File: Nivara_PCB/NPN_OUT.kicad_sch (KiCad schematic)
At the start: 0 parts

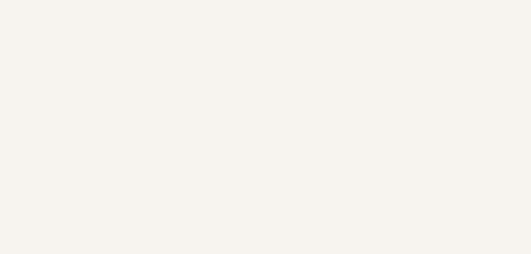
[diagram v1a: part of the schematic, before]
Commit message: Añadido de funciones NPN/PNP
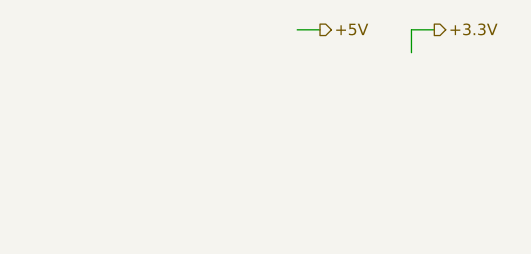
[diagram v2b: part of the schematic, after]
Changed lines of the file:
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@@
 	(generator_version "9.0")
 	(paper "A4")
+	(wire
+		(pts
+			(xy 104.14 50.8) (xy 104.14 53.34)
+		)
+		(stroke
+			(width 0)
+			(type default)
+		)
+	)
+	(wire
+		(pts
+			(xy 91.44 50.8) (xy 93.98 50.8)
+		)
+		(stroke
+			(width 0)
+			(type default)
+		)
+	)
+	(wire
+		(pts
+			(xy 106.68 50.8) (xy 104.14 50.8)
+		)
+		(stroke
+			(width 0)
+			(type default)
+		)
+	)
+	(hierarchical_label "+5V"
+		(shape output)
+		(at 93.98 50.8 0)
+		(effects
+			(font
+				(size 1.27 1.27)
+			)
+			(justify left)
+		)
+	)
+	(hierarchical_label "+3.3V"
+		(shape output)
+		(at 106.68 50.8 0)
+		(effects
+			(font
+				(size 1.27 1.27)
+			)
+			(justify left)
+		)
+	)
 	(hierarchical_label "NPN_OUT_1"
 		(shape output)

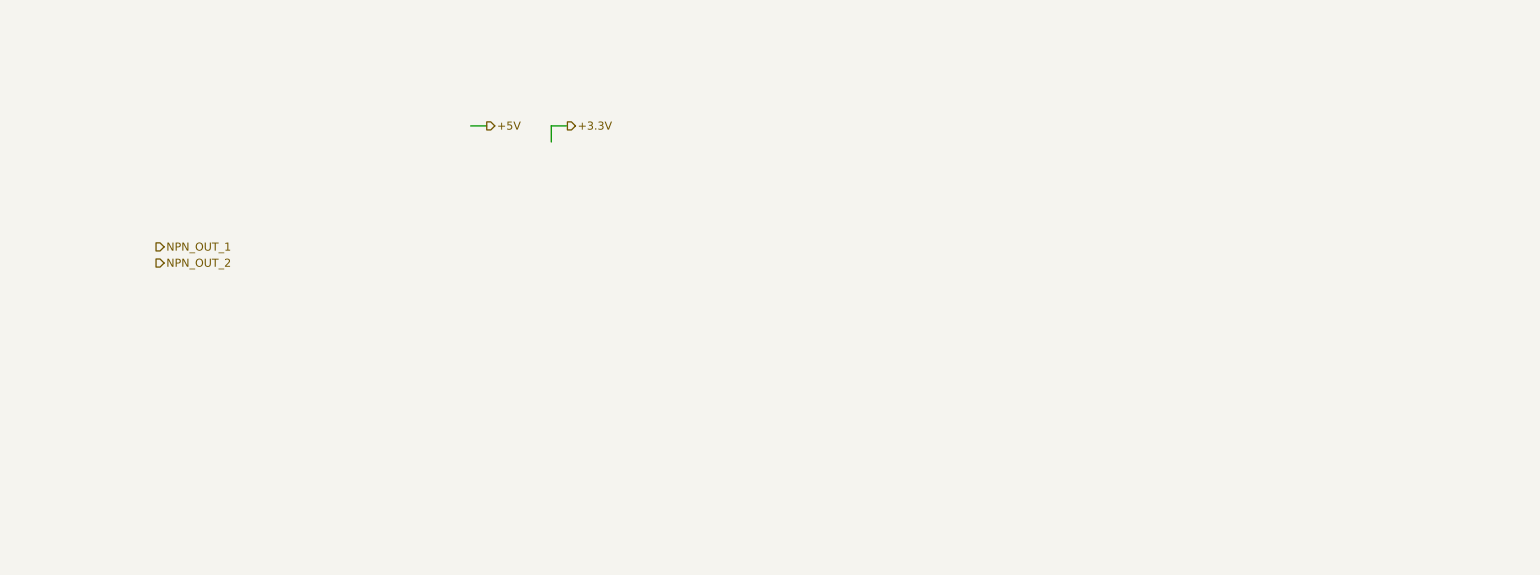
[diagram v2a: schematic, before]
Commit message: Cambios en el esquema de NPN y PNP
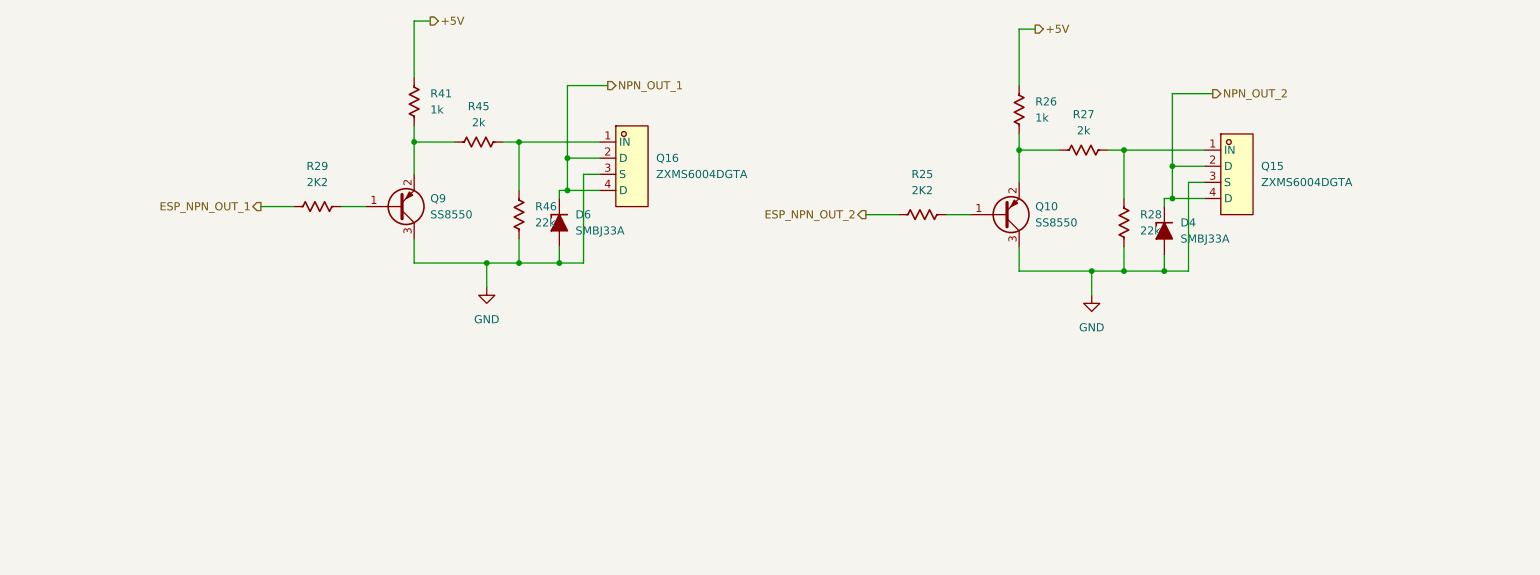
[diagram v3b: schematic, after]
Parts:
- added D4, D6: SMBJ33A, PCM_Diode_SMD_AKL:D_SMB, symbol PCM_Diode_TVS_AKL:SMBJ33A
- added Q10, Q9: SS8550, Package_TO_SOT_SMD:SOT-23, symbol Transistor_BJT:SS8550
- added Q15, Q16: ZXMS6004DGTA, Fuse_Holder:SOT-223-3_L6.5-W3.4-P2.30-LS7.0-BR, symbol Fuse_Holder:ZXMS6004DGTA
- added R25, R29: 2K2, PCM_Resistor_SMD_AKL:R_0603_1608Metric, symbol PCM_Resistor_US_AKL:R_0603
- added R26, R41: 1k, PCM_Resistor_SMD_AKL:R_0603_1608Metric, symbol PCM_Resistor_US_AKL:R_0603
- added R27, R45: 2k, PCM_Resistor_SMD_AKL:R_0603_1608Metric, symbol PCM_Resistor_US_AKL:R_0603
- added R28, R46: 22k, PCM_Resistor_SMD_AKL:R_0603_1608Metric, symbol PCM_Resistor_US_AKL:R_0603
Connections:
- net +5V: now also R26.1, R41.1
- net NPN_OUT_1: now also D6.1 (K), Q16.2 (D), Q16.4 (D)
- net NPN_OUT_2: now also D4.1 (K), Q15.2 (D), Q15.4 (D)
- new net: Q10.1 (B), R25.2
- new net: Q9.1 (B), R29.2
- new net: Q9.2 (E), R41.2, R45.1
- new net: Q16.1 (IN), R45.2, R46.2
- new net: Q15.1 (IN), R27.2, R28.2
- new net: Q10.2 (E), R26.2, R27.1
- new net ESP_NPN_OUT_1: R29.1
- new net ESP_NPN_OUT_2: R25.1
- new net GND: D4.2 (A), D6.2 (A), Q10.3 (C), Q15.3 (S), Q16.3 (S), Q9.3 (C), R28.1, R46.1

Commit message: Cambio de IntelliFet, porque los que tenían no estaban disponibles.
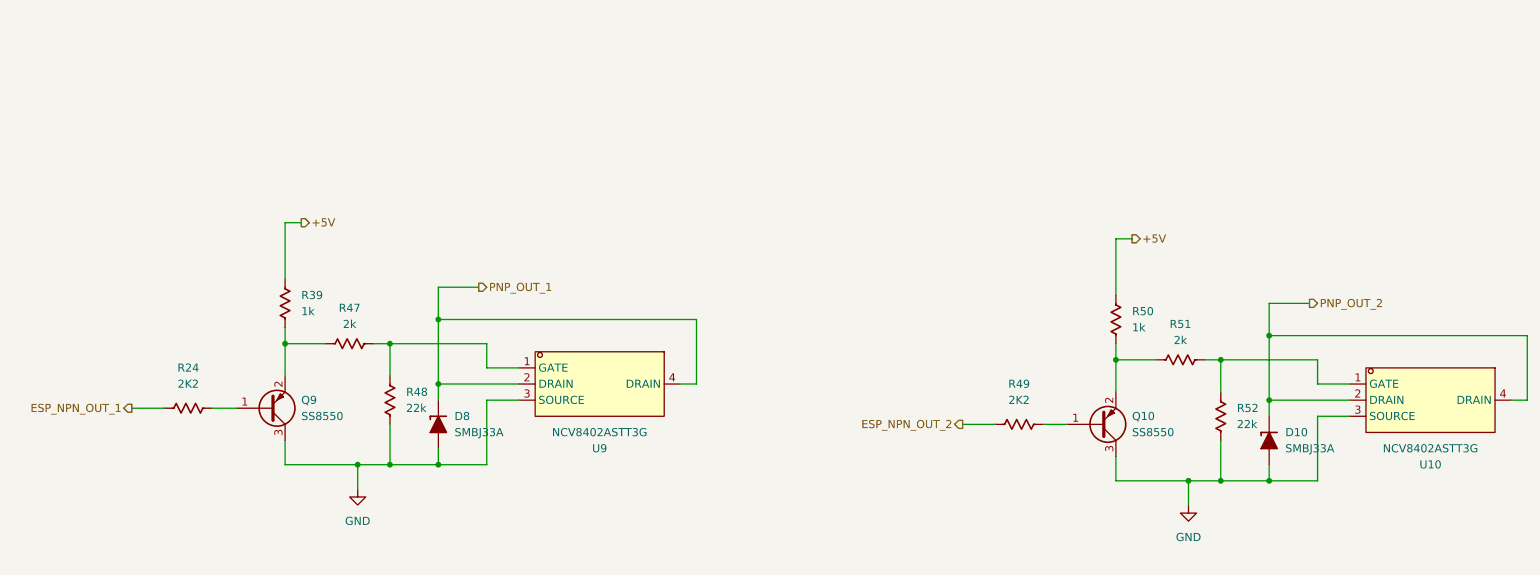
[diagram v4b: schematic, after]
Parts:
- removed D4, D6: SMBJ33A, PCM_Diode_SMD_AKL:D_SMB, symbol PCM_Diode_TVS_AKL:SMBJ33A
- removed Q15, Q16: ZXMS6004DGTA, Fuse_Holder:SOT-223-3_L6.5-W3.4-P2.30-LS7.0-BR, symbol Fuse_Holder:ZXMS6004DGTA
- removed R25, R29: 2K2, PCM_Resistor_SMD_AKL:R_0603_1608Metric, symbol PCM_Resistor_US_AKL:R_0603
- removed R26, R41: 1k, PCM_Resistor_SMD_AKL:R_0603_1608Metric, symbol PCM_Resistor_US_AKL:R_0603
- removed R27, R45: 2k, PCM_Resistor_SMD_AKL:R_0603_1608Metric, symbol PCM_Resistor_US_AKL:R_0603
- removed R28, R46: 22k, PCM_Resistor_SMD_AKL:R_0603_1608Metric, symbol PCM_Resistor_US_AKL:R_0603
- added D10, D8: SMBJ33A, PCM_Diode_SMD_AKL:D_SMB, symbol PCM_Diode_TVS_AKL:SMBJ33A
- added R24, R49: 2K2, PCM_Resistor_SMD_AKL:R_0603_1608Metric, symbol PCM_Resistor_US_AKL:R_0603
- added R39, R50: 1k, PCM_Resistor_SMD_AKL:R_0603_1608Metric, symbol PCM_Resistor_US_AKL:R_0603
- added R47, R51: 2k, PCM_Resistor_SMD_AKL:R_0603_1608Metric, symbol PCM_Resistor_US_AKL:R_0603
- added R48, R52: 22k, PCM_Resistor_SMD_AKL:R_0603_1608Metric, symbol PCM_Resistor_US_AKL:R_0603
- added U10, U9: NCV8402ASTT3G, Fuse_Holder:SOT-223_L6.5-W3.5-P2.30-LS7.0-BR, symbol Fuse_Holder:NCV8402ASTT3G
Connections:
- net +5V: now also R39.1, R50.1
- net ESP_NPN_OUT_1: now also R24.1
- net ESP_NPN_OUT_2: now also R49.1
- net GND: now also D10.2 (A), D8.2 (A), R48.1, R52.1, U10.3 (SOURCE), U9.3 (SOURCE)
- net at Q10.1 (B): now also R49.2
- net at Q9.1 (B): now also R24.2
- net at Q9.2 (E): now also R39.2, R47.1
- net at Q10.2 (E): now also R50.2, R51.1
- new net: R47.2, R48.2, U9.1 (GATE)
- new net: R51.2, R52.2, U10.1 (GATE)
- new net PNP_OUT_1: D8.1 (K), U9.2 (DRAIN), U9.4 (DRAIN)
- new net PNP_OUT_2: D10.1 (K), U10.2 (DRAIN), U10.4 (DRAIN)
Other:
- moved on the sheet: Q10, Q9

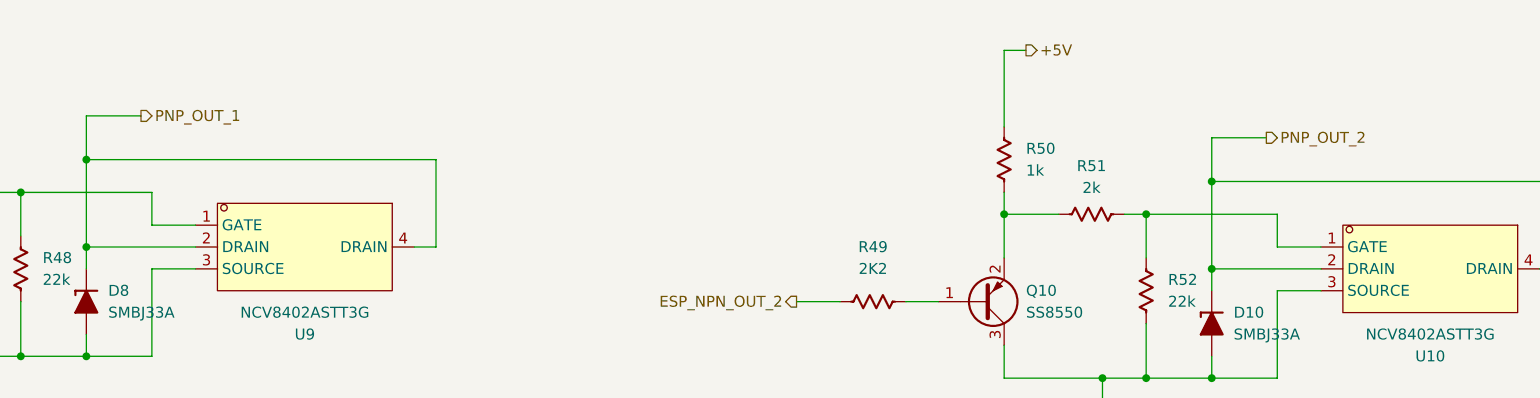
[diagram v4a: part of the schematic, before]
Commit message: Cambios en las mediciones análogas.
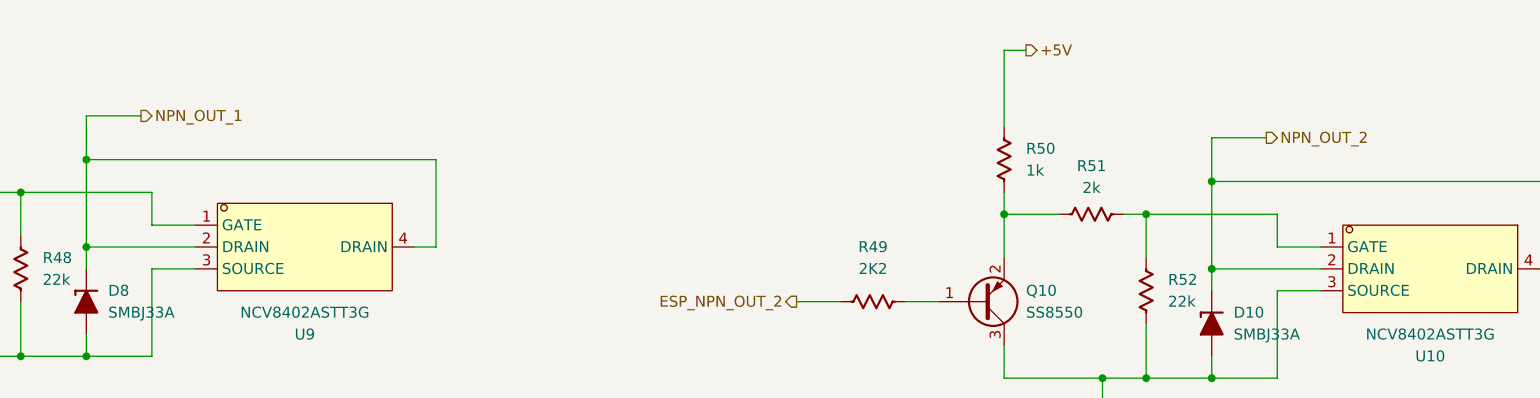
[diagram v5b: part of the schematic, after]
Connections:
- net PNP_OUT_1 renamed NPN_OUT_1
- net PNP_OUT_2 renamed NPN_OUT_2
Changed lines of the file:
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@@
 		)
 	)
-	(hierarchical_label "PNP_OUT_1"
+	(hierarchical_label "NPN_OUT_1"
 		(shape output)
 		(at 92.71 76.2 0)
@@
 		)
 	)
-	(hierarchical_label "PNP_OUT_2"
+	(hierarchical_label "NPN_OUT_2"
 		(shape output)
 		(at 223.52 78.74 0)

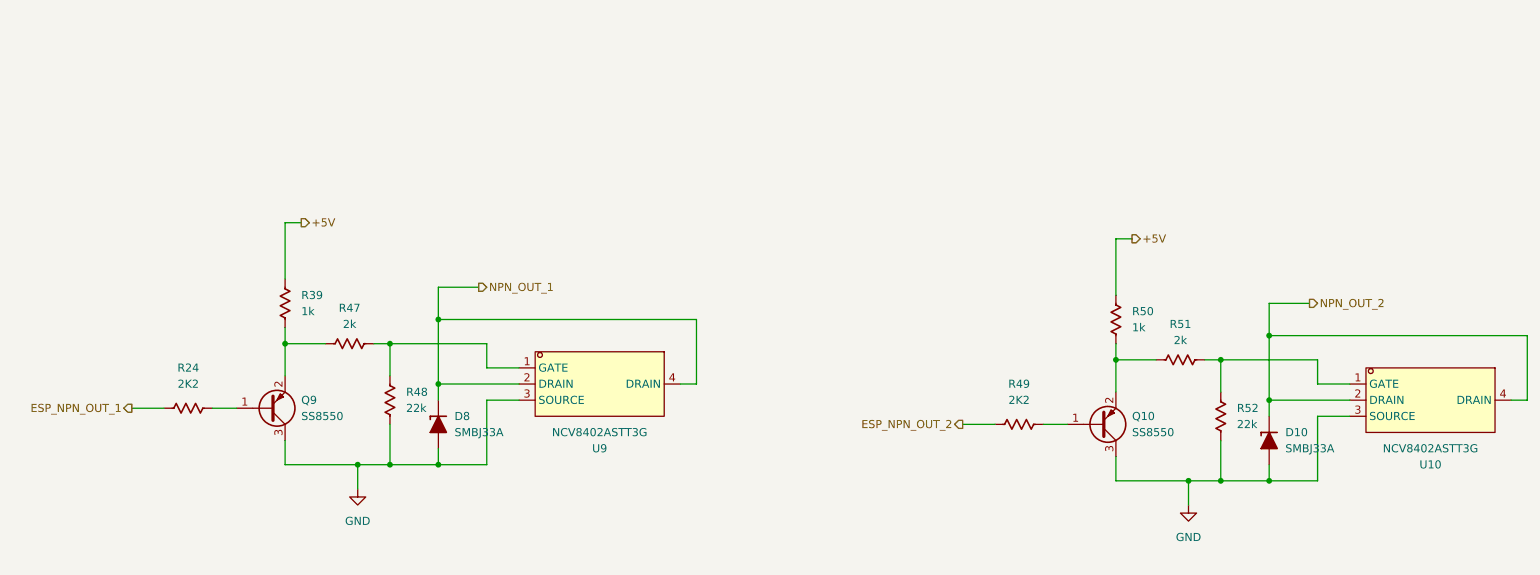
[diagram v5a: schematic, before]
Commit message: Cambios en las salidas analogicas, ya que el ESP32 S3 no tiene DAC
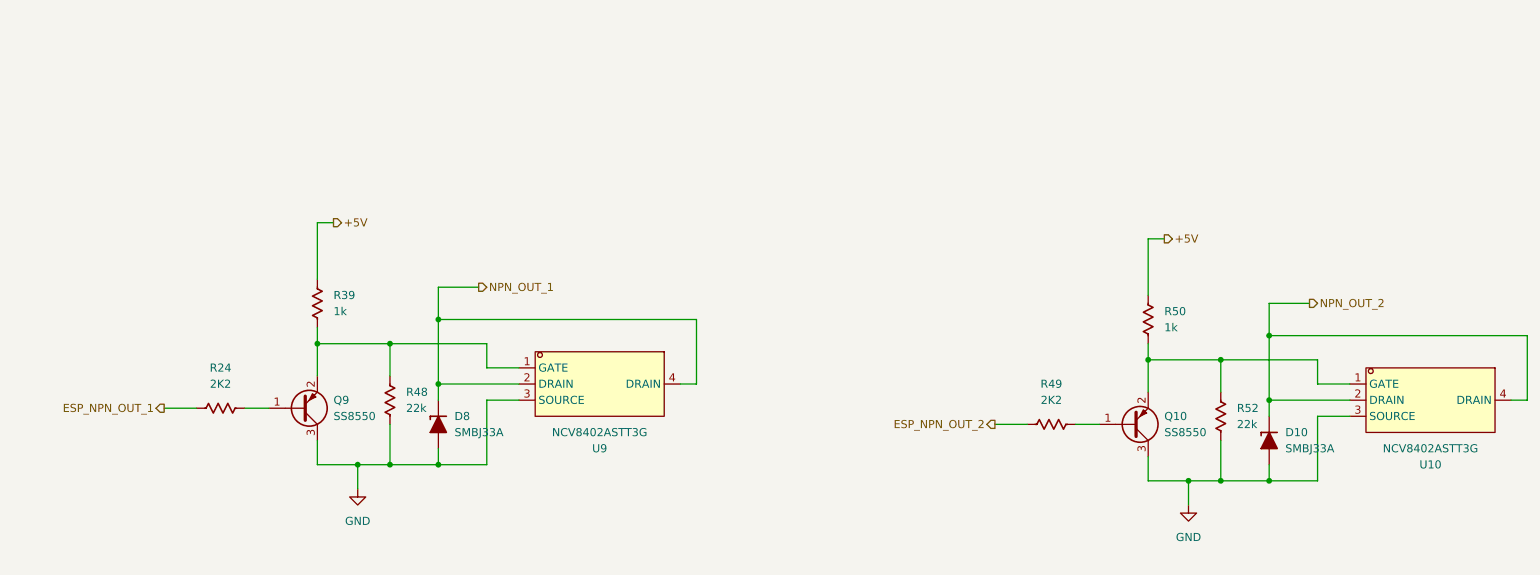
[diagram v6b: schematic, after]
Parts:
- removed R47, R51: 2k, PCM_Resistor_SMD_AKL:R_0603_1608Metric, symbol PCM_Resistor_US_AKL:R_0603
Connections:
- net at R48.2, U9.1 (GATE): now also Q9.2 (E), R39.2
- net at R52.2, U10.1 (GATE): now also Q10.2 (E), R50.2
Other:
- moved on the sheet: Q10, Q9, R24, R39, R49, R50

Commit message: Cambios en la medición de voltaje y corriente de la PCB Nivara.
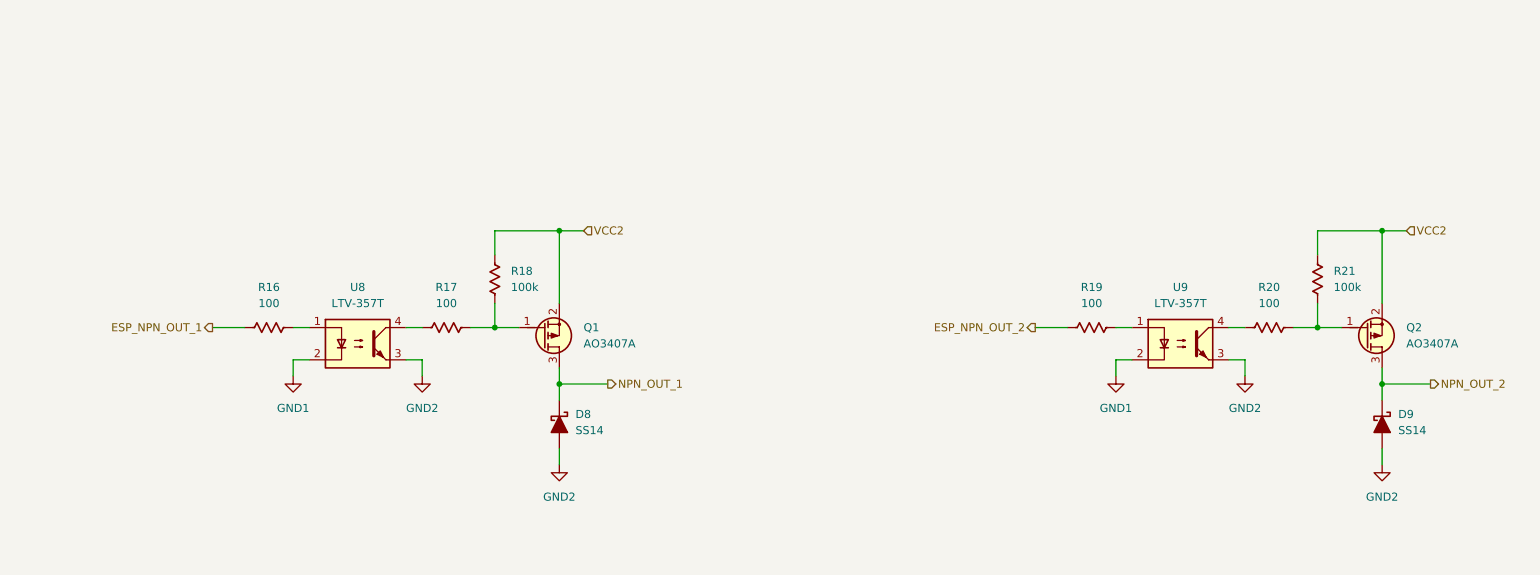
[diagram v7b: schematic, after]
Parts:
- removed D10, D8: SMBJ33A, PCM_Diode_SMD_AKL:D_SMB, symbol PCM_Diode_TVS_AKL:SMBJ33A
- removed Q10, Q9: SS8550, Package_TO_SOT_SMD:SOT-23, symbol Transistor_BJT:SS8550
- removed R49: 2K2, PCM_Resistor_SMD_AKL:R_0603_1608Metric, symbol PCM_Resistor_US_AKL:R_0603
- removed R50: 1k, PCM_Resistor_SMD_AKL:R_0603_1608Metric, symbol PCM_Resistor_US_AKL:R_0603
- removed R52: 22k, PCM_Resistor_SMD_AKL:R_0603_1608Metric, symbol PCM_Resistor_US_AKL:R_0603
- removed U10, U9: NCV8402ASTT3G, Fuse_Holder:SOT-223_L6.5-W3.5-P2.30-LS7.0-BR, symbol Fuse_Holder:NCV8402ASTT3G
- added D8, D9: SS14, PCM_Diode_SMD_AKL:D_SMA, symbol PCM_Diode_Schottky_AKL:SS14
- added Q1, Q2: AO3407A, PCM_Package_TO_SOT_SMD_AKL:SOT-23, symbol PCM_Transistor_MOSFET_AKL:AO3407A
- added R19, R20: 100, PCM_Resistor_SMD_AKL:R_0603_1608Metric, symbol PCM_Resistor_US_AKL:R_0603
- added R21: 100k, PCM_Resistor_SMD_AKL:R_0603_1608Metric, symbol PCM_Resistor_US_AKL:R_0603
- added U8, U9: LTV-357T, Package_SO:SO-4_4.4x3.6mm_P2.54mm, symbol Isolator:LTV-357T
- R16: renamed from R24; value 2K2 -> 100
- R17: renamed from R48; value 22k -> 100
- R18: renamed from R39; value 1k -> 100k
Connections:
- net GND is gone; now on an unnamed net: R17.1
- net ESP_NPN_OUT_2: now also R19.1
- net NPN_OUT_1: now also D8.1 (K), Q1.3 (D)
- net NPN_OUT_2: now also D9.1 (K), Q2.3 (D)
- net at R18.2: now also Q1.1 (G); no longer R17.2
- net at R16.2: now also U8.1
- net +5V renamed VCC2
- net VCC2: now also Q1.2 (S), Q2.2 (S), R21.1
- new net: Q2.1 (G), R20.1, R21.2
- new net: R20.2, U9.4
- new net: R17.2, U8.4
- new net: R19.2, U9.1
- new net GND1: U8.2, U9.2
- new net GND2: D8.2 (A), D9.2 (A), U8.3, U9.3
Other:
- moved on the sheet: R16, R17, R18

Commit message: New changes to the Nivara PCB schematic files.
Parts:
- added D27, D28: LED ON, LED_SMD:LED_0603_1608Metric, symbol Device:LED
- added R54, R55: 1.5k, PCM_Resistor_SMD_AKL:R_0603_1608Metric, symbol PCM_Resistor_US_AKL:R_0603
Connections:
- net GND2: now also D27.1 (K), D28.1 (K)
- net NPN_OUT_1: now also R54.1
- net NPN_OUT_2: now also R55.1
- new net: D28.2 (A), R55.2
- new net: D27.2 (A), R54.2
